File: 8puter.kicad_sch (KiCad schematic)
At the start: 32 parts, among them J1 PWR-DC, U1 74AC00, X1 ECS-2200BX-100

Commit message: small updates
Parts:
- DEBUG1: value (none) -> Conn_02x16_Odd_Even; footprint (none) -> Connector_PinHeader_2.54mm:PinHeader_2x16_P2.54mm_Vertical
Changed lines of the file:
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@@
       (effects (font (size 1.27 1.27)) (justify left))
     )
-    (property "Value" "" (id 1) (at 217.17 149.2249 90)
+    (property "Value" "Conn_02x16_Odd_Even" (id 1) (at 217.17 149.2249 90)
       (effects (font (size 1.27 1.27)) (justify left))
     )
-    (property "Footprint" "" (id 2) (at 237.49 149.225 0)
+    (property "Footprint" "Connector_PinHeader_2.54mm:PinHeader_2x16_P2.54mm_Vertical" (id 2) (at 237.49 149.225 0)
       (effects (font (size 1.27 1.27)) hide)
     )

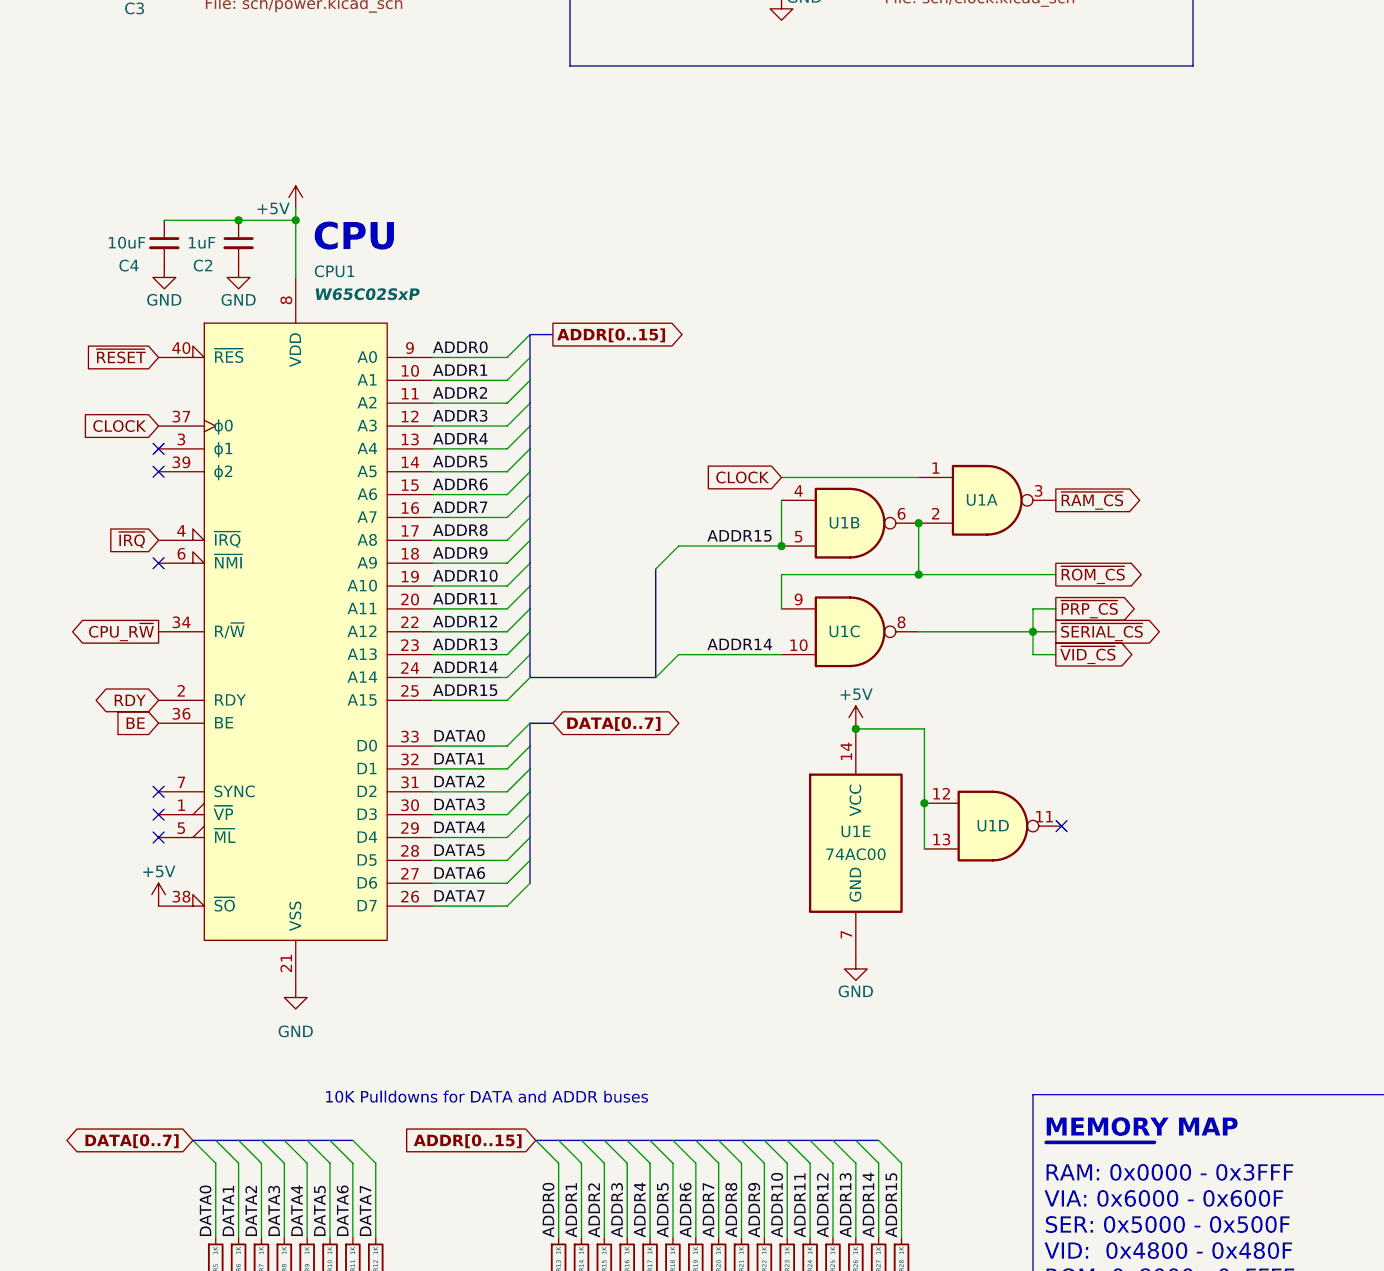
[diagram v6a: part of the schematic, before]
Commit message: Comments in Sch
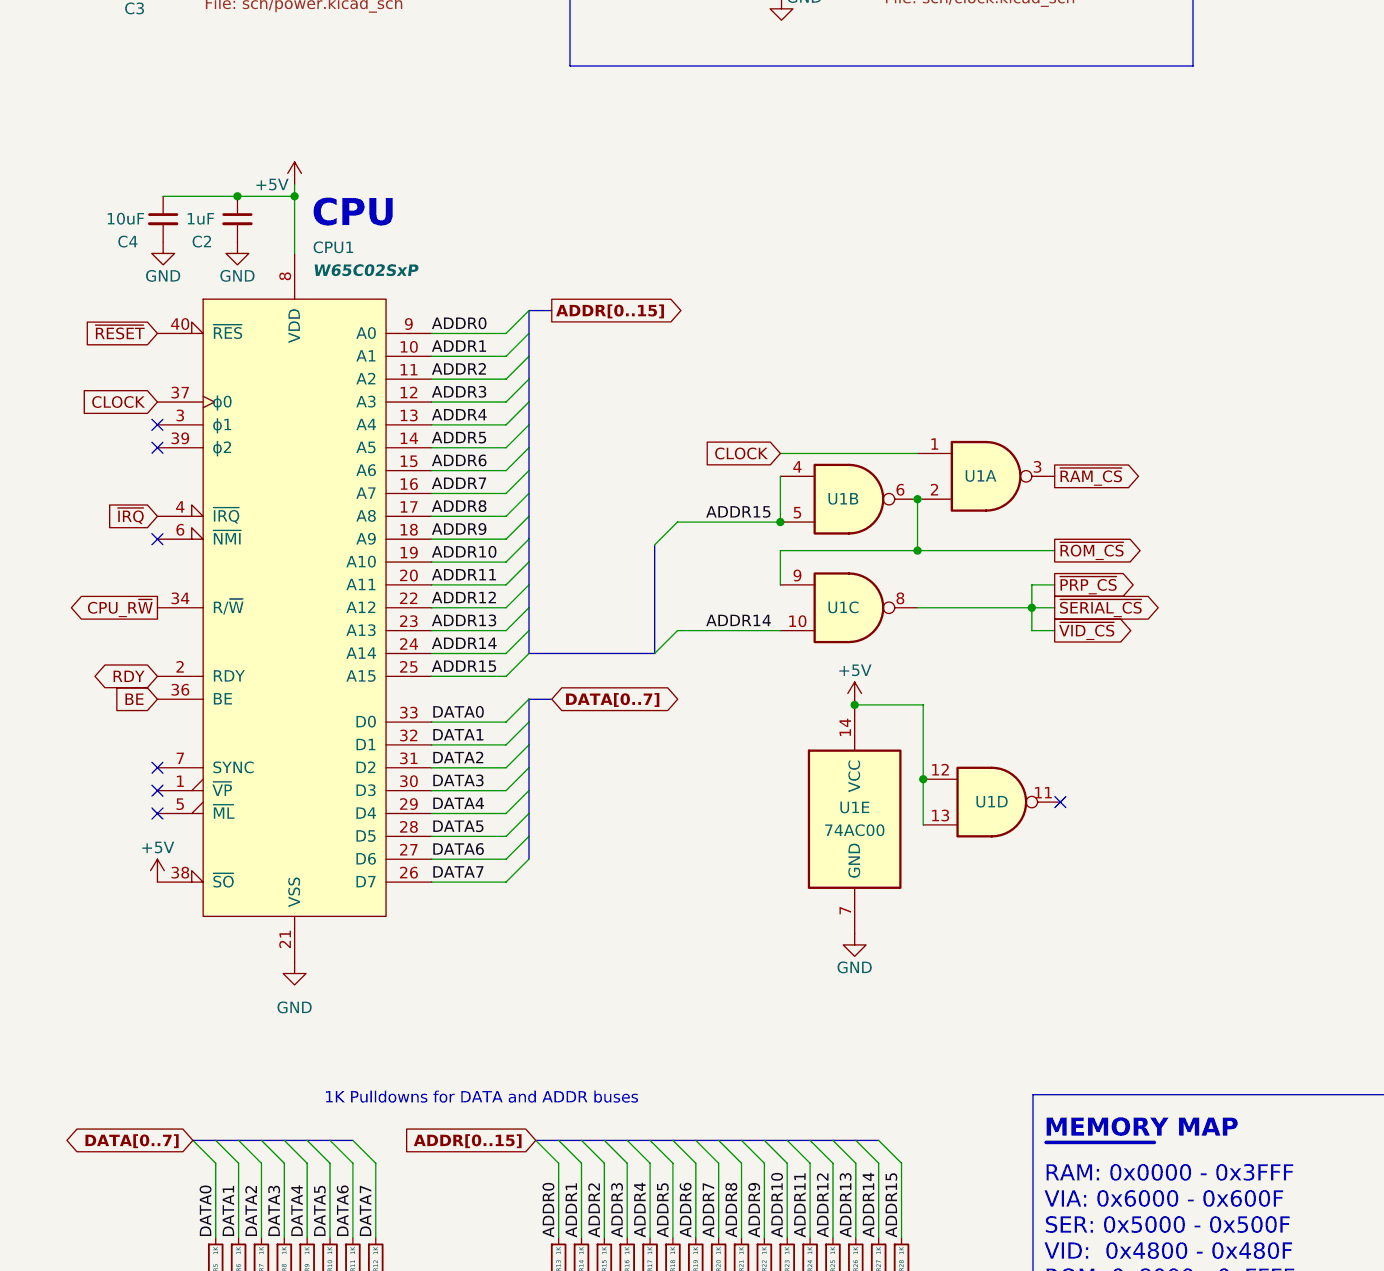
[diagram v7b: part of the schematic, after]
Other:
- note added: "1K Pulldowns for DATA and ADDR buses"
- note removed: "10K Pulldowns for DATA and ADDR buses"
- moved on the sheet: C2, C4, CPU1, U1A, U1B, U1C, U1D, U1E
